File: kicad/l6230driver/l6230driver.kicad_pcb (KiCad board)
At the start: 2 copper layers, 57 parts, among them J1 Conn_01x02_Female, J2 Conn_01x03_Female, J3 Conn_01x01_Female, J4 Conn_01x02_Female, J5 Conn_01x02_Female, J6 Conn_01x02_Female, J7 Conn_01x04_Female, J8 Conn_01x02_Female, J9 Conn_01x04_Female, U1 L6230PD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

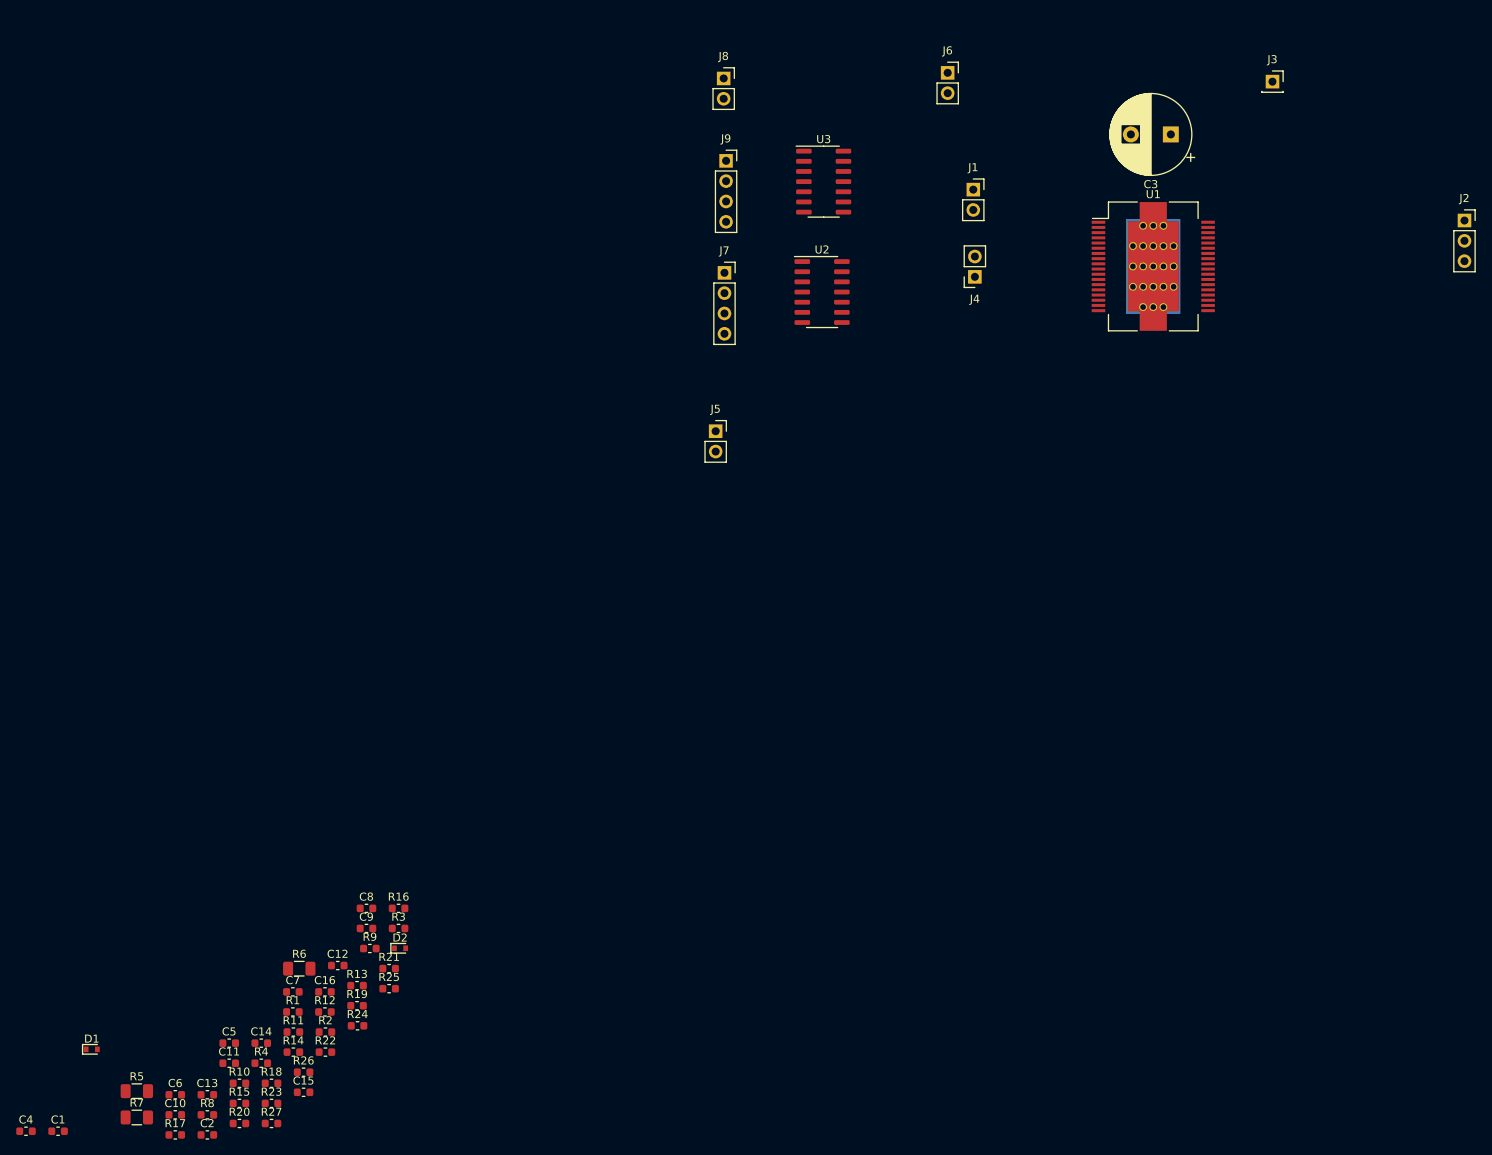
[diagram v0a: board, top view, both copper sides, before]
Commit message: schematics + placing
Signed-off-by: Martin Egli <eglidev@gmx.net>
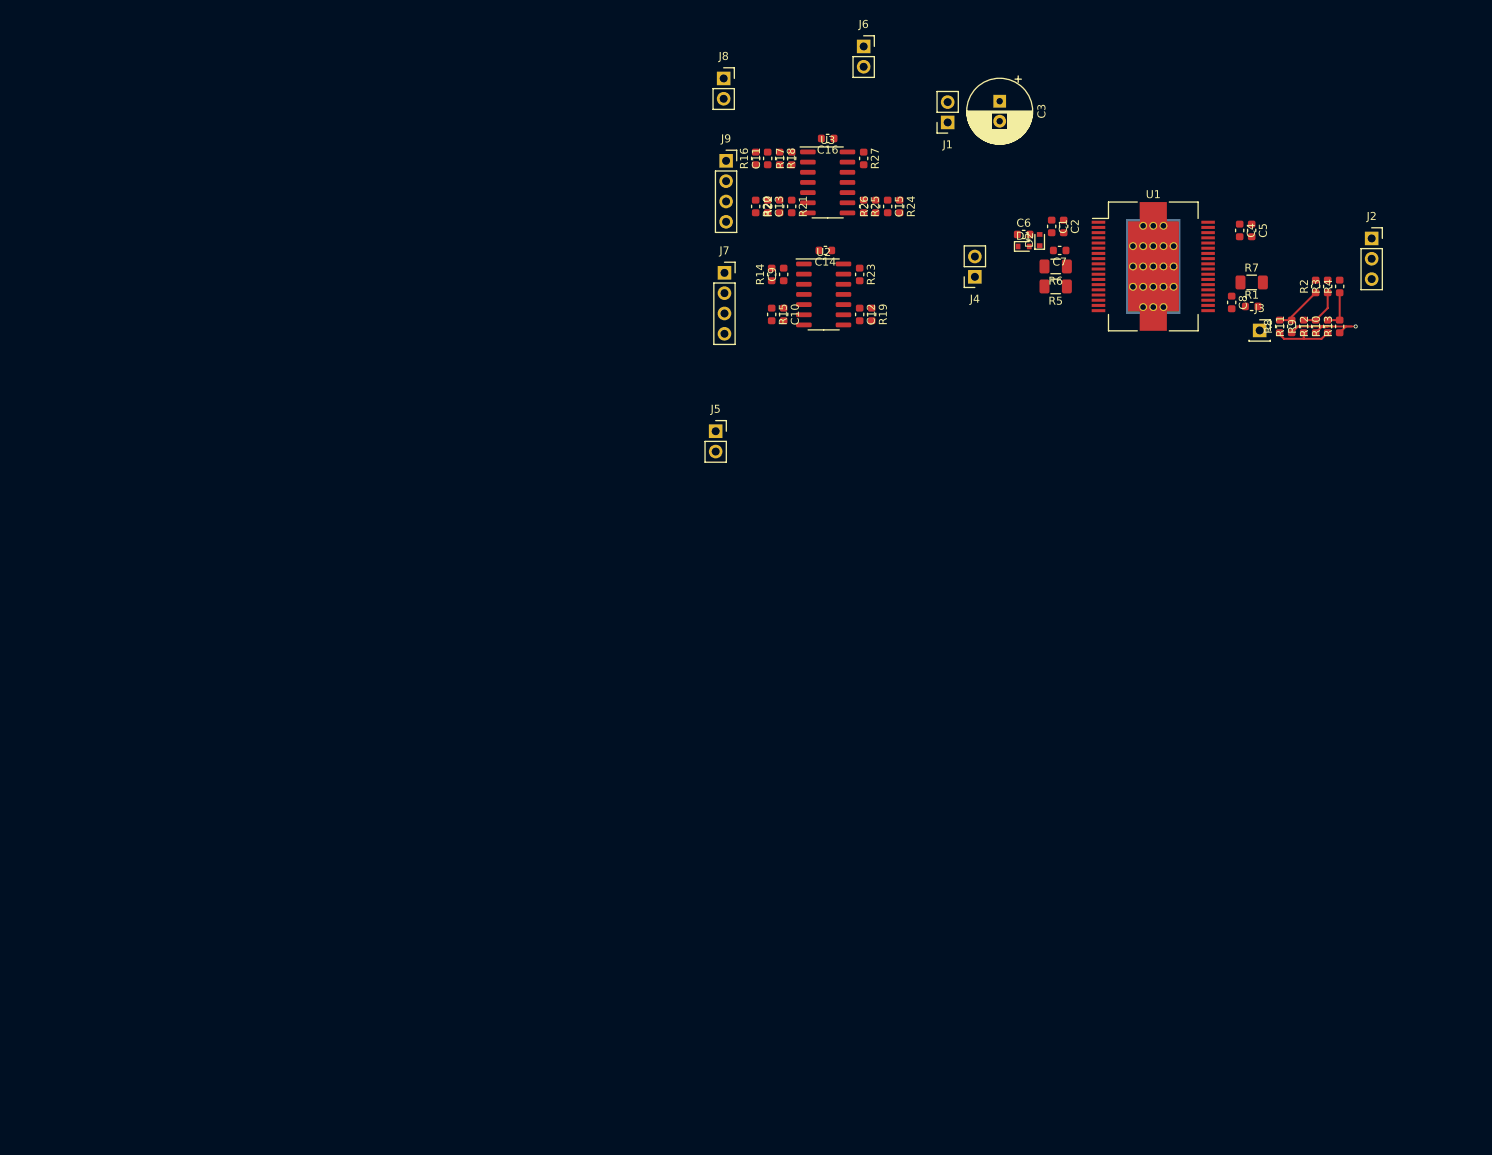
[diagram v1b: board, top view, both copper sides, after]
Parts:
- C3: footprint Capacitor_THT:CP_Radial_D10.0mm_P5.00mm -> Capacitor_THT:CP_Radial_D8.0mm_P2.50mm
- moved C4 188.9 mm to (186.5, 68.0), turned to -90 degrees
- moved R7 174.1 mm to (188.0, 74.5)
- moved C1 168.0 mm to (163.0, 67.5), turned to -90 degrees
- moved R8 166.4 mm to (191.5, 80.0), turned to 90 degrees
- moved R4 166.1 mm to (199.0, 75.0), turned to 90 degrees
- moved R10 165.7 mm to (197.5, 80.0), turned to 90 degrees
- moved C5 163.3 mm to (188.0, 68.0), turned to -90 degrees
- moved C2 156.1 mm to (164.5, 67.5), turned to -90 degrees
- moved R2 154.9 mm to (196.0, 75.0), turned to 90 degrees
- moved D1 153.8 mm to (159.5, 70.0)
- moved R11 152.8 mm to (193.0, 80.0), turned to 90 degrees
- moved R5 152.7 mm to (163.5, 75.0), turned to 180 degrees
- moved C6 151.0 mm to (159.5, 68.5)
- moved R12 150.6 mm to (196.0, 80.0), turned to 90 degrees
- moved R1 148.8 mm to (188.0, 77.5)
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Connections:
- C1 pad 2: Net-(C1-Pad2) -> VS
- C10 pad 1: /V_1 -> Net-(U2-Pad5)
- C11 pad 1: /U_SENS -> Net-(C11-Pad1)
- C12 pad 1: /W_1 -> Net-(C12-Pad1)
- C13 pad 1: /V_SENS -> Net-(C13-Pad1)
- C15 pad 1: /W_SENS -> Net-(U3-Pad10)
- C2 pad 2: Net-(C1-Pad2) -> VS
- C3 pad 1: Net-(C1-Pad2) -> VS
- C4 pad 2: Net-(C1-Pad2) -> VS
- C5 pad 2: Net-(C1-Pad2) -> VS
- C6 pad 2: Net-(C6-Pad2) -> VS
- C9 pad 1: /U_1 -> Net-(C9-Pad1)
- D2 pad 2: Net-(C6-Pad2) -> VS
- J1 pad 2: Net-(C1-Pad2) -> VS
- R14 pad 1: /U_1 -> Net-(C9-Pad1)
- R14 pad 2: Net-(R14-Pad2) -> /U_1
- R15 pad 1: /V_1 -> Net-(U2-Pad5)
- R15 pad 2: Net-(R15-Pad2) -> /V_1
- R16 pad 1: /U_SENS -> Net-(C11-Pad1)
- R16 pad 2: Net-(R16-Pad2) -> /U_SENS
- R19 pad 1: /W_1 -> Net-(C12-Pad1)
- R19 pad 2: Net-(R19-Pad2) -> /W_1
- R20 pad 1: /V_SENS -> Net-(C13-Pad1)
- R20 pad 2: Net-(R20-Pad2) -> /V_SENS
- R24 pad 1: /W_SENS -> Net-(U3-Pad10)
- R24 pad 2: Net-(R24-Pad2) -> /W_SENS
- U1 pad 13: Net-(U1-Pad13) -> unconnected-(U1-Pad13)
- U1 pad 14: Net-(U1-Pad14) -> unconnected-(U1-Pad14)
- U1 pad 16: Net-(U1-Pad16) -> unconnected-(U1-Pad16)
- U1 pad 17: Net-(U1-Pad17) -> unconnected-(U1-Pad17)
- U1 pad 2: Net-(U1-Pad2) -> unconnected-(U1-Pad2)
- U1 pad 20: Net-(U1-Pad20) -> unconnected-(U1-Pad20)
- U1 pad 21: Net-(U1-Pad21) -> unconnected-(U1-Pad21)
- U1 pad 23: Net-(U1-Pad23) -> unconnected-(U1-Pad23)
- U1 pad 24: Net-(U1-Pad24) -> unconnected-(U1-Pad24)
- U1 pad 28: Net-(U1-Pad28) -> unconnected-(U1-Pad28)
- U1 pad 3: Net-(U1-Pad3) -> unconnected-(U1-Pad3)
- U1 pad 31: Net-(U1-Pad31) -> unconnected-(U1-Pad31)
- U1 pad 33: Net-(C1-Pad2) -> VS
- U1 pad 34: Net-(U1-Pad34) -> unconnected-(U1-Pad34)
- U1 pad 35: Net-(U1-Pad35) -> unconnected-(U1-Pad35)
- U1 pad 37: (no net) -> GND
- U1 pad 4: Net-(C1-Pad2) -> VS
- U1 pad 6: Net-(C7-Pad1) -> unconnected-(U1-Pad6)
- U1 pad 7: (no net) -> Net-(C7-Pad1)
- U2 pad 10: Net-(R19-Pad2) -> Net-(C12-Pad1)
- U2 pad 3: Net-(R14-Pad2) -> Net-(C9-Pad1)
- U2 pad 5: Net-(R15-Pad2) -> Net-(U2-Pad5)
- U3 pad 10: Net-(R24-Pad2) -> Net-(U3-Pad10)
- U3 pad 3: Net-(R16-Pad2) -> Net-(C11-Pad1)
- U3 pad 5: Net-(R20-Pad2) -> Net-(C13-Pad1)
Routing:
- net GND: track 0.00 -> 12.0 mm, vias 0 -> 1
- net /VIRT_N: track 0.00 -> 7.54 mm
- net /U_1: track 0.00 -> 6.17 mm
- net /V_1: track 0.00 -> 5.55 mm
- net /W_1: track 0.00 -> 4.93 mm
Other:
- net class Default removed

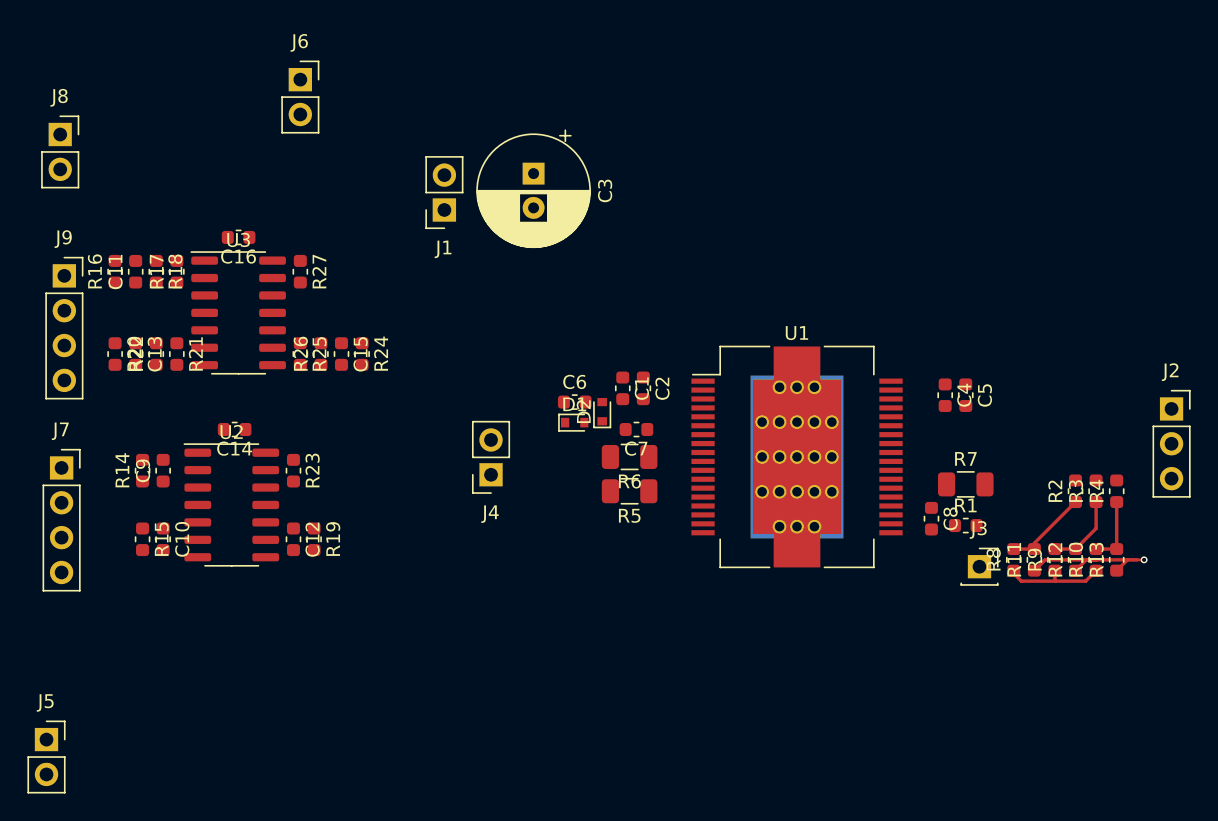
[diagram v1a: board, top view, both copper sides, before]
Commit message: added HSOP-36 footprint to own pritty-lib, placing, routing
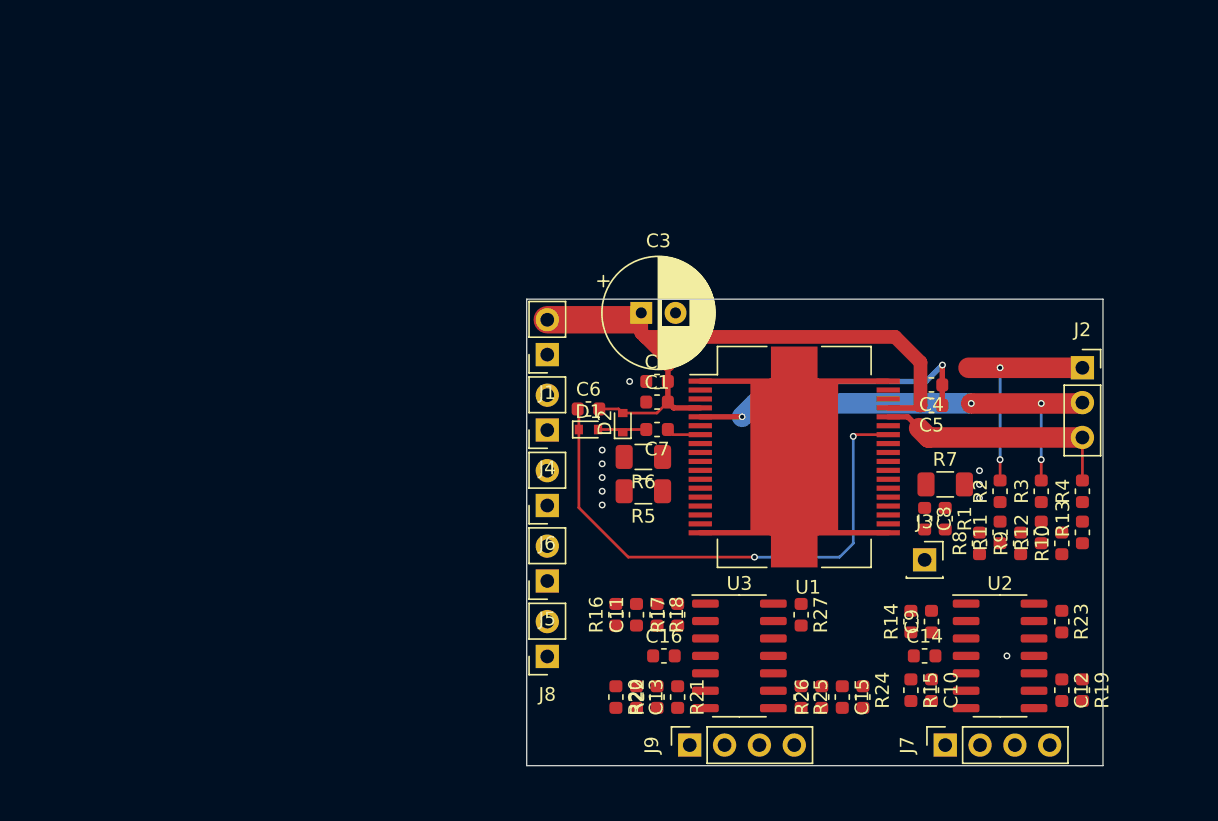
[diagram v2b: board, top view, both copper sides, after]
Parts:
- U1: footprint Package_SO:HSOP-36-1EP_11.0x15.9mm_P0.65mm_SlugDown_ThermalVias -> L6230:HSOP-36
- moved J7 67.5 mm to (186.5, 93.5), turned to 90 degrees
- moved C10 57.1 mm to (185.5, 89.5)
- moved C12 57.1 mm to (195.0, 89.5)
- moved C9 57.1 mm to (185.5, 84.5)
- moved R14 57.1 mm to (184.0, 84.5)
- moved R15 57.1 mm to (184.0, 89.5)
- moved R19 57.1 mm to (196.5, 89.5)
- moved R23 57.1 mm to (195.0, 84.5)
- moved U2 57.1 mm to (190.5, 87.0)
- moved J9 57.0 mm to (167.9, 93.5), turned to 90 degrees
- moved C14 52.9 mm to (185.0, 87.0), turned to 0 degrees
- moved J8 52.0 mm to (157.5, 87.0), turned to 180 degrees
- moved C11 44.2 mm to (164.0, 84.0)
- moved C13 44.2 mm to (164.0, 90.0)
- moved C15 44.2 mm to (179.0, 90.0)
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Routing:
- net VS: track 0.00 -> 48.8 mm
- net Net-(C6-Pad1): track 0.00 -> 39.5 mm, vias 0 -> 2
- net /V: track 0.00 -> 33.9 mm, vias 0 -> 4
- net GND: track 12.0 -> 36.2 mm, vias 1 -> 11
- net /W: track 0.00 -> 17.9 mm
- net /U: track 0.00 -> 16.5 mm, vias 0 -> 2
- net /VIRT_N: track 7.54 -> 0.00 mm
- net /U_1: track 6.17 -> 0.00 mm
- net /V_1: track 5.55 -> 0.00 mm
- net /W_1: track 4.93 -> 0.00 mm
- net Net-(C7-Pad2): track 0.00 -> 3.51 mm
- net Net-(C7-Pad1): track 0.00 -> 2.52 mm
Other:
- board outline added: 42 x 34 mm

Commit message: 100% routed
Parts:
- turned R15 to 90 degrees
- turned R19 to 90 degrees
- turned R20 to 90 degrees
- turned R24 to 90 degrees
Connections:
- J9 pad 1: Net-(J9-Pad1) -> Net-(R21-Pad2)
- J9 pad 2: Net-(J9-Pad2) -> Net-(R17-Pad2)
- R17 pad 2: Net-(J9-Pad1) -> Net-(R17-Pad2)
- R21 pad 2: Net-(J9-Pad2) -> Net-(R21-Pad2)
- U1 pad 28: unconnected-(U1-Pad28) -> GND
- U3 pad 1: Net-(J9-Pad1) -> Net-(R17-Pad2)
- U3 pad 7: Net-(J9-Pad2) -> Net-(R21-Pad2)
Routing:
- net GND: track 36.2 -> 101.7 mm, vias 11 -> 31
- net +3V3: track 0.00 -> 50.9 mm, vias 0 -> 5
- net Net-(J5-Pad1): track 0.00 -> 28.6 mm, vias 0 -> 1
- net Net-(J6-Pad1): track 0.00 -> 28.3 mm, vias 0 -> 1
- net Net-(J5-Pad2): track 0.00 -> 27.8 mm, vias 0 -> 1
- net /V_1: track 0.00 -> 24.4 mm, vias 0 -> 2
- net /VIRT_N: track 0.00 -> 23.8 mm
- net /V_SENS: track 0.00 -> 22.3 mm
- net /U: track 16.5 -> 38.2 mm, vias 2 -> 3
- net /W_SENS: track 0.00 -> 19.5 mm, vias 0 -> 2
- net Net-(J7-Pad1): track 0.00 -> 16.1 mm
- net /W_1: track 0.00 -> 15.4 mm
- net Net-(J4-Pad2): track 0.00 -> 14.3 mm, vias 0 -> 2
- net Net-(R17-Pad2): track 0.00 -> 13.7 mm
- net Net-(J4-Pad1): track 0.00 -> 12.9 mm, vias 0 -> 2
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- added copper zone on B.Cu, net GND
